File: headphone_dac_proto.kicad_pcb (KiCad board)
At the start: 2 copper layers, 75.5 x 62.5 mm, 66 parts, among them J1 USB_B_Mini, J2 Conn_02x10_Odd_Even, J3 Conn_02x05_Odd_Even, J6 6.35mm, U1 LT3042xMSE, U2 CY8C5888LTI-LP097, U3 CS4344, U4 TPA6139A2, Y1 Crystal_GND24

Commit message: More cleanup
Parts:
- J2: value Conn_02x10_Odd_Even -> Bluetooth
- J3: value Conn_02x05_Odd_Even -> Prog
- J6: value 6.35mm -> Headphones
- moved R10 11.5 mm to (150.5, 127.2)
- moved J2 2.77 mm to (99.8, 96.8)
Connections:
- U2 pad 61: /bt_cts -> Net-(U2-Pad61)
- U2 pad 62: /bt_rts -> Net-(U2-Pad62)
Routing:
- net /bt_cts: track 38.3 -> 0.00 mm, vias 1 -> 0
- net /bt_rts: track 37.8 -> 0.00 mm, vias 1 -> 0
- net Net-(J1-Pad6): track 23.2 -> 3.43 mm
- net /sw3: track 46.1 -> 39.6 mm
- net /sw1: track 34.3 -> 27.8 mm
- net /sw2: track 35.1 -> 28.6 mm
- net Net-(R10-Pad1): track 11.5 -> 6.52 mm, vias 1 -> 0
- net /bt_tx: track 28.3 -> 29.9 mm, vias 0 -> 1
- net /bt_rx: track 29.1 -> 30.6 mm, vias 0 -> 1
- net GND: track 105.3 -> 106.0 mm
- net /~mute~: track 24.5 -> 25.1 mm
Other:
- outline, holes or cut-outs redrawn
- board text removed: "THE VOID"

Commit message: Change programming connector. Finish BOM
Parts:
- J3: value Prog -> Conn_01x05_Male; footprint conn_prog:FTSH-105 -> Connector_PinHeader_2.54mm:PinHeader_1x05_P2.54mm_Vertical
- Y1: value Crystal_GND24 -> 12.288MHz
- moved J3 4.85 mm to (108.8, 111.2), turned to 90 degrees
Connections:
- net /tck renamed /swdck
- J3 pad 2: /tms -> GND
- J3 pad 3: GND -> /xres
- J3 pad 5: GND -> /swdio
- U2 pad 11: /tms -> /swdio
- U2 pad 14: /tdo -> Net-(U2-Pad14)
- U2 pad 15: /tdi -> Net-(U2-Pad15)
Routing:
- net /tms: track 16.3 -> 0.00 mm
- net /tdo: track 14.0 -> 0.00 mm
- net /tdi: track 12.9 -> 0.00 mm
- net /swdio: track 0.00 -> 11.0 mm
- net /xres: track 26.1 -> 17.6 mm
- net GND: track 106.0 -> 103.2 mm, vias 41 -> 40
- net /swdck: track 15.3 -> 13.1 mm
- net +3V3: track 76.2 -> 77.9 mm

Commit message: Update labels
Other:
- board text added: "Half-Spin Headphone DAC Proto V1.0 2020-07-03"
- board text added: "No Earbuds Allowed. Hi-Fi Cans Only."
- board text added: "This text reduces THD by 0.001%"
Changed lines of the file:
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@@
   (general
     (thickness 1.6)
-    (drawings 10)
+    (drawings 13)
     (tracks 422)
     (zones 0)
@@
     (tags "Potentiometer vertical Bourns PTV09A-1 Single")
     (zone_connect 0)
-    (fp_text reference RV3 (at 11 -10 90) (layer F.SilkS)
+    (fp_text reference RV3 (at -1.75 3 180) (layer F.SilkS)
       (effects (font (size 1 1) (thickness 0.15)))
     )
@@
     (tags "Potentiometer vertical Bourns PTV09A-1 Single")
     (zone_connect 0)
-    (fp_text reference RV2 (at 11 -10 90) (layer F.SilkS)
+    (fp_text reference RV2 (at -1.75 3 180) (layer F.SilkS)
       (effects (font (size 1 1) (thickness 0.15)))
     )
@@
     (tags "Potentiometer vertical Bourns PTV09A-1 Single")
     (zone_connect 0)
-    (fp_text reference RV1 (at 11 -10.15 90) (layer F.SilkS)
+    (fp_text reference RV1 (at -1.75 3 180) (layer F.SilkS)
       (effects (font (size 1 1) (thickness 0.15)))
     )
@@
     )
   )
+  (gr_text "No Earbuds Allowed.\nHi-Fi Cans Only." (at 150.5 149.5) (layer F.SilkS)
+    (effects (font (size 1 1) (thickness 0.15)))
+  )
+  (gr_text "This text reduces\nTHD by 0.001%" (at 156 106.25) (layer F.SilkS)
+    (effects (font (size 1 1) (thickness 0.15)))
+  )
+  (gr_text "Half-Spin\nHeadphone DAC Proto V1.0\n2020-07-03" (at 102.25 132.25) (layer F.SilkS)
+    (effects (font (size 1 1) (thickness 0.15)))
+  )
   (gr_arc (start 92 96) (end 92 92.5) (angle -90) (layer Edge.Cuts) (width 0.05))

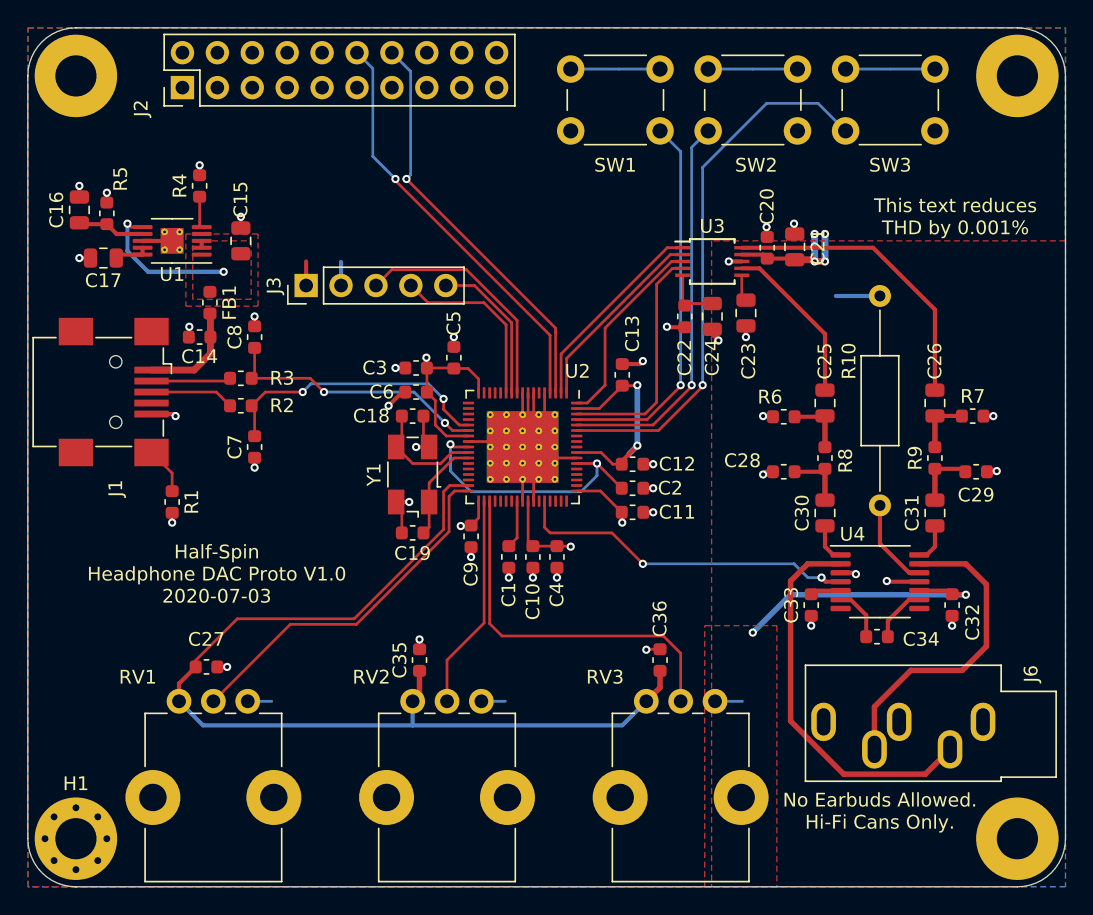
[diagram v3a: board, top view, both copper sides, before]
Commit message: Add logos and links. #networking
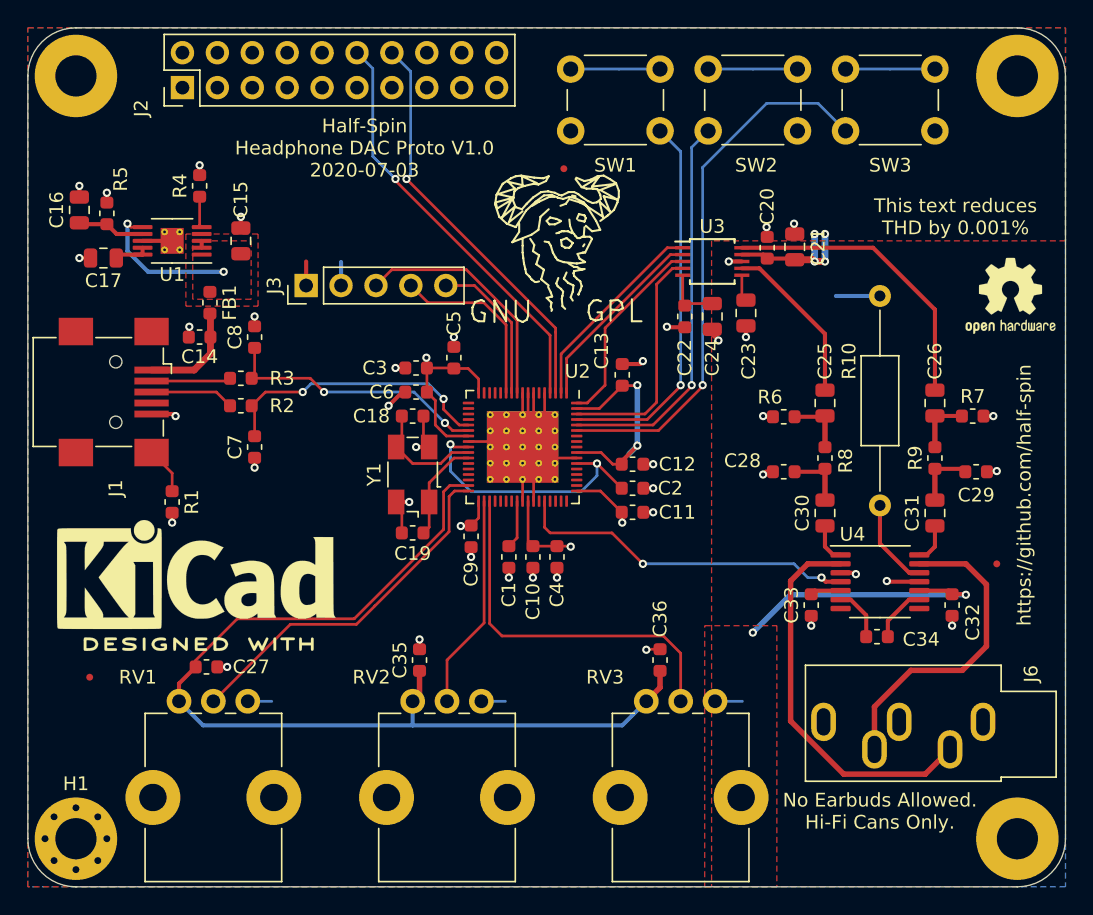
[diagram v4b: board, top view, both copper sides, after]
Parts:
- added FID1: ~, Fiducial:Fiducial_0.5mm_Mask1.5mm, F.Cu at (93.0, 139.8)
- added FID2: ~, Fiducial:Fiducial_0.5mm_Mask1.5mm, F.Cu at (159.0, 131.5)
- added FID3: ~, Fiducial:Fiducial_0.5mm_Mask1.5mm, F.Cu at (127.5, 102.8)
- added REF**: Symbol_GNU-Logo_SilkscreenTop, Symbol:Symbol_GNU-Logo_SilkscreenTop, F.Cu at (127.2, 107.0)
- added REF**: OSHW-Logo2_7.3x6mm_SilkScreen, Symbol:OSHW-Logo2_7.3x6mm_SilkScreen, F.Cu at (160.0, 112.0)
- added REF**: KiCad-Logo2_8mm_SilkScreen, Symbol:KiCad-Logo2_8mm_SilkScreen, F.Cu at (100.8, 132.2)
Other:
- board text added: "https://github.com/half-spin"
